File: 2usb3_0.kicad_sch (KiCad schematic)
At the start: 11 parts, among them J5 2xUSB3.0, U3 AP22615AWU

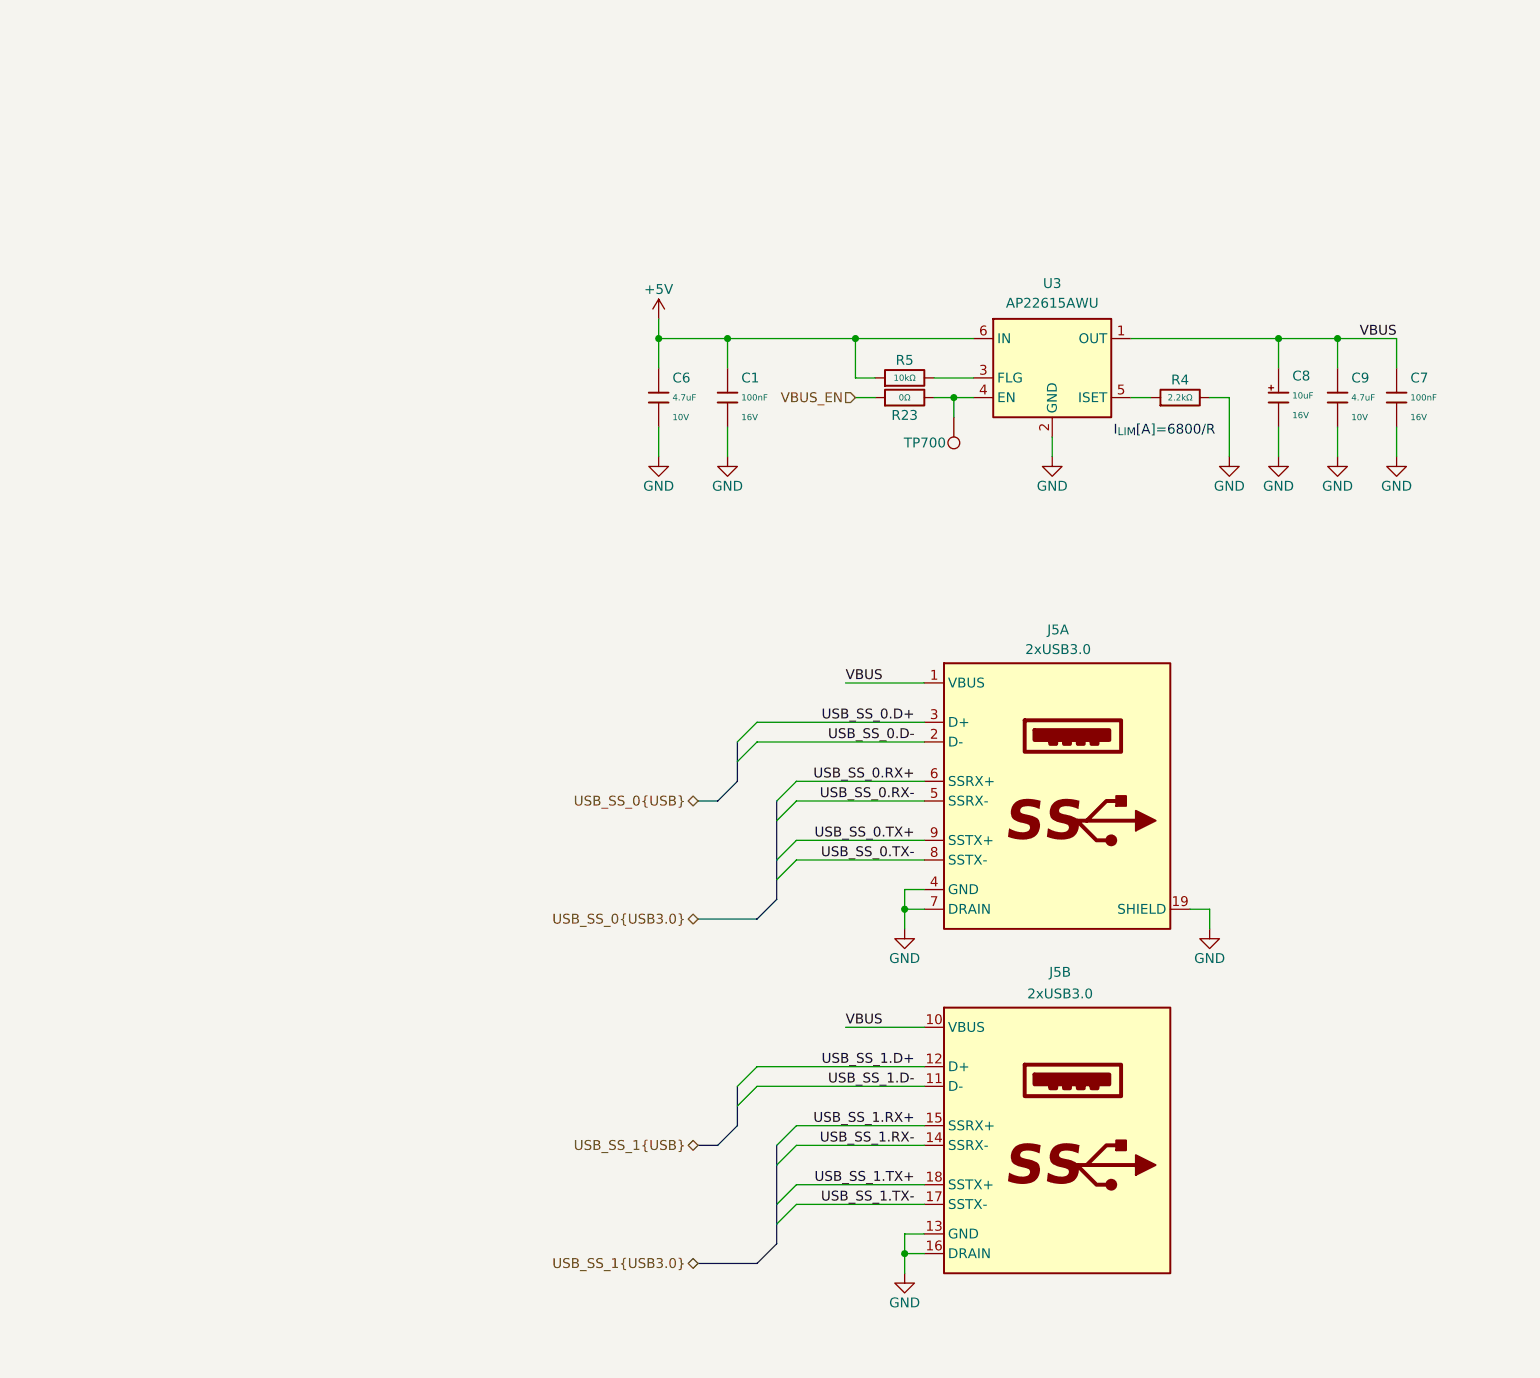
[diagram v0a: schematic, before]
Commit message: [#1] WIP: Change components to ones from the global library, refactor schematic
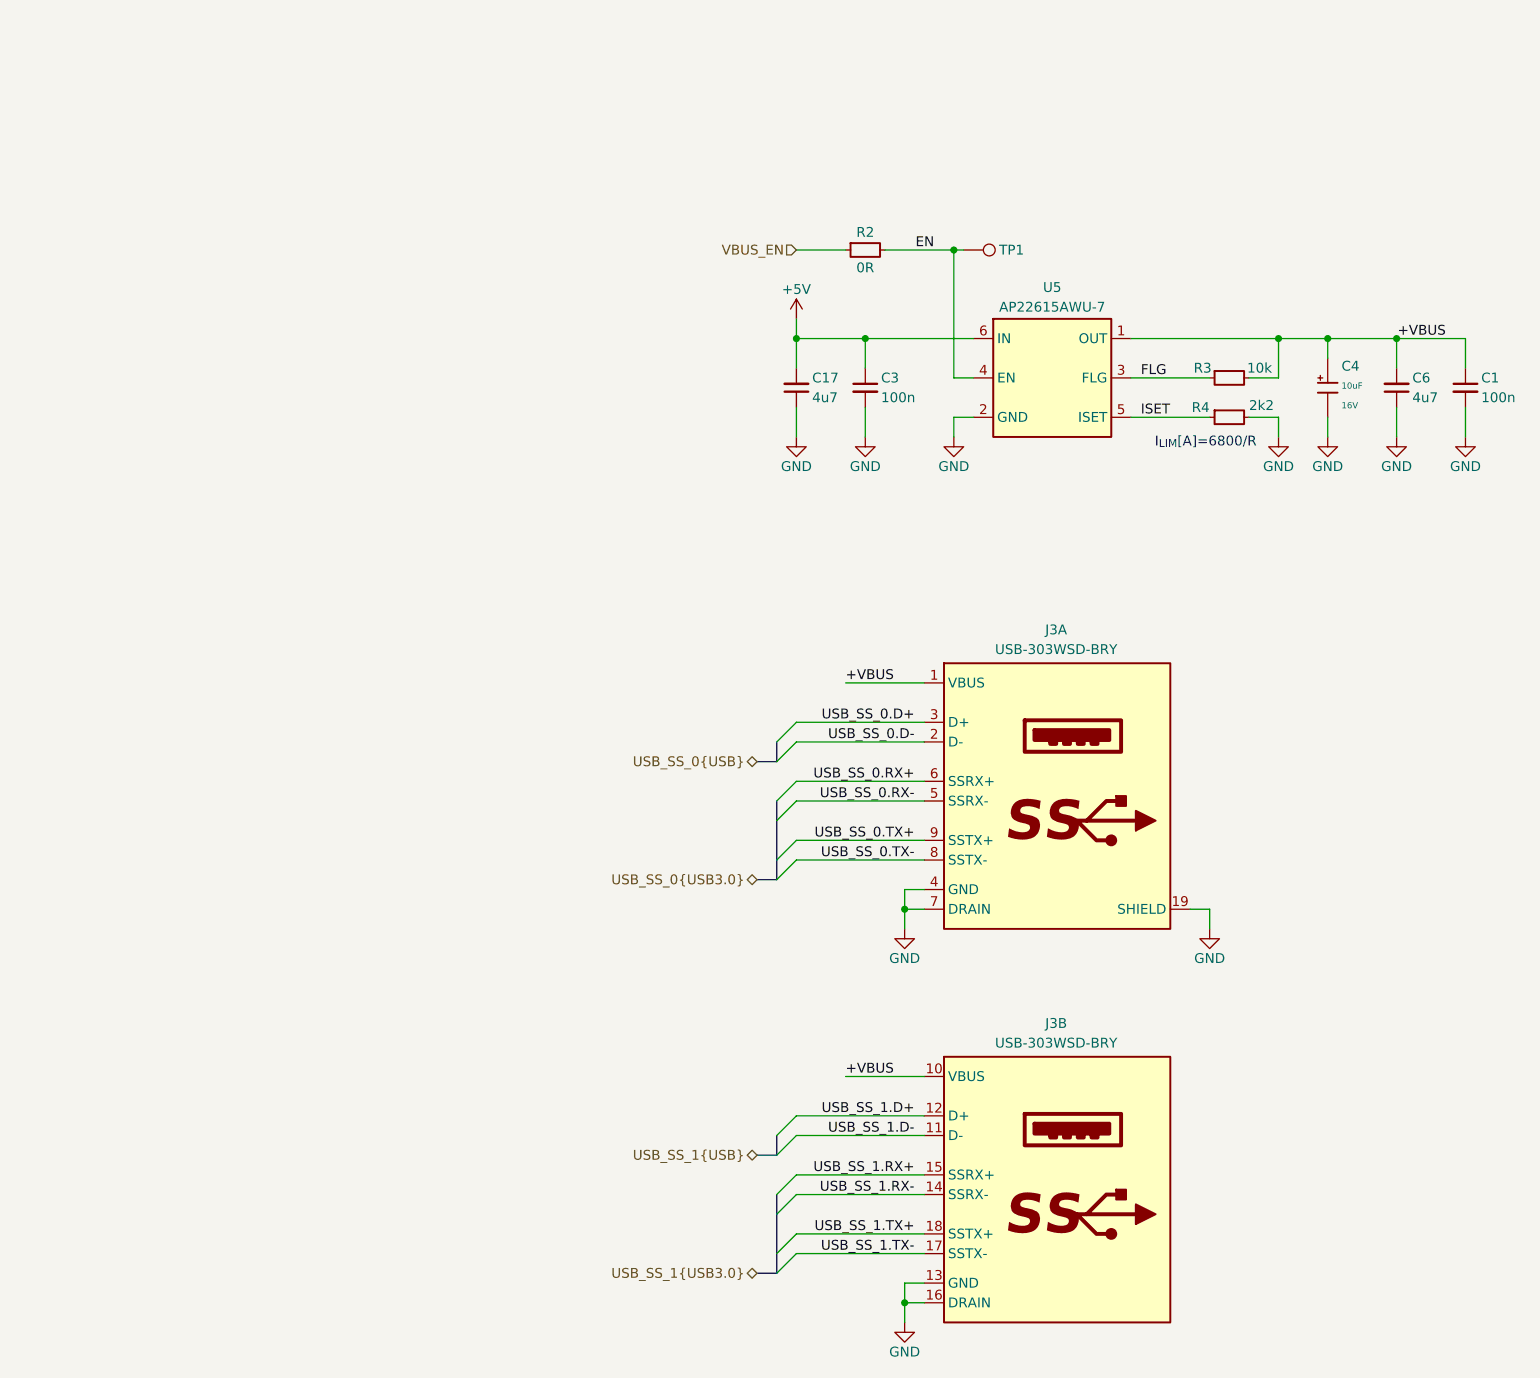
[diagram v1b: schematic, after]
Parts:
- removed C1, C7: 100nF, PCM_JLCPCB:C_0402, symbol PCM_JLCPCB-Capacitors:0402,100nF
- removed C6, C9: 4.7uF, PCM_JLCPCB:C_0402, symbol PCM_JLCPCB-Capacitors:0402,4.7uF
- removed J5: 2xUSB3.0, lib:2xUSB3.0-USB-303WSD-BRY, symbol connectors:2xUSB3.0-USB-303WSD-BRY
- removed R23: 0Ω, PCM_JLCPCB:R_0402, symbol PCM_JLCPCB-Resistors:0402,0Ω
- removed R4: 2.2kΩ, PCM_JLCPCB:R_0402, symbol PCM_JLCPCB-Resistors:0402,2.2kΩ
- removed R5: 10kΩ, PCM_JLCPCB:R_0402, symbol PCM_JLCPCB-Resistors:0402,10kΩ
- removed U3: AP22615AWU, Package_TO_SOT_SMD:SOT-23-6, symbol Regulator_Linear:AP22615AWU
- added C1, C3: C-100n-0402, DW-footprints:C_0402_1005Metric, symbol DW-capacitors:C-100n-0402
- added C17, C6: C-4u7-0402, DW-footprints:C_0402_1005Metric, symbol DW-capacitors:C-4u7-0402
- added J3: USB-A_USB-303WSD-BRY, DW-footprints:USB-A_Receptacle_USB-303WSD-BRY, symbol DW-connectors:USB-A_USB-303WSD-BRY
- added R2: R-0R-0402, DW-footprints:R_0402_1005Metric, symbol DW-resistors:R-0R-0402
- added R3: R-10k-0402, DW-footprints:R_0402_1005Metric, symbol DW-resistors:R-10k-0402
- added R4: R-2k2-0402, DW-footprints:R_0402_1005Metric, symbol DW-resistors:R-2k2-0402
- added U5: AP22615AWU-7, DW-footprints:TSOT-23-6, symbol DW-ICs:AP22615AWU-7
- renumbered C8 to C4, TP700 to TP1
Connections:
- net +5V: now also C17.2, C3.1, U5.6 (IN)
- net GND: now also C1.2, C17.1, C3.2, C6.1, J3.13 (GND), J3.16 (DRAIN), J3.19 (SHIELD), J3.4 (GND), J3.7 (DRAIN), R4.2, U5.2 (GND)
- net USB_SS_0.D+: now also J3.3 (D+)
- net USB_SS_0.D-: now also J3.2 (D-)
- net USB_SS_0.RX+: now also J3.6 (SSRX+)
- net USB_SS_0.RX-: now also J3.5 (SSRX-)
- net USB_SS_0.TX+: now also J3.9 (SSTX+)
- net USB_SS_0.TX-: now also J3.8 (SSTX-)
- net USB_SS_1.D+: now also J3.12 (D+)
- net USB_SS_1.D-: now also J3.11 (D-)
- net USB_SS_1.RX+: now also J3.15 (SSRX+)
- net USB_SS_1.RX-: now also J3.14 (SSRX-)
- net USB_SS_1.TX+: now also J3.18 (SSTX+)
- net USB_SS_1.TX-: now also J3.17 (SSTX-)
- net VBUS_EN: now also R2.1
- net EN: now reaches TP1.1
- net EN: now also R2.2, U5.4 (EN)
- net VBUS renamed +VBUS
- net +VBUS: now also C1.1, C6.2, J3.1 (VBUS), J3.10 (VBUS), R3.2, U5.1 (OUT)
- new net FLG: R3.1, U5.3 (FLG)
- new net ISET: R4.1, U5.5 (ISET)
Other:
- moved on the sheet: C4, TP1

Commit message: [#1] Re-annotate schematic
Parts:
- removed TP1: TestPoint, TestPoint:TestPoint_Pad_D1.0mm, symbol Connector:TestPoint
- added TP7: TP_SMD_0.75mm, DW-footprints:TP_SMD_0.75mm, symbol DW-test-points:TP_SMD_0.75mm
- renumbered C1 to C4, C4 to C5, C17 to C6, C6 to C7, J3 to J7, R2 to R10, R3 to R11, R4 to R12, U5 to U1
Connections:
- net EN: now also TP7.1
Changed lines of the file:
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@@
 		(on_board yes)
 		(dnp no)
-		(property "Reference" "#PWR24"
+		(property "Reference" "#PWR034"
 			(at 199.39 90.17 0)
 			(effects
@@
 			(project "cm5-module"
 				(path "/090a8e41-87a8-4fb1-998b-60a2c0dc4cee/658b004a-eb7c-4ad1-a8df-d1cd97b62092"
-					(reference "#PWR24")
+					(reference "#PWR034")
 					(unit 1)
 				)
@@
 		(on_board yes)
 		(dnp no)
-		(property "Reference" "R2"
+		(property "Reference" "R10"
 			(at 199.39 57.404 0)
 			(effects
@@
 			(project ""
 				(path "/090a8e41-87a8-4fb1-998b-60a2c0dc4cee/658b004a-eb7c-4ad1-a8df-d1cd97b62092"
-					(reference "R2")
+					(reference "R10")
 					(unit 1)
 				)
@@
 		(on_board yes)
 		(dnp no)
-		(property "Reference" "#PWR25"
+		(property "Reference" "#PWR035"
 			(at 210.82 90.17 0)
 			(effects
@@
 			(project "cm5-module"
 				(path "/090a8e41-87a8-4fb1-998b-60a2c0dc4cee/658b004a-eb7c-4ad1-a8df-d1cd97b62092"
-					(reference "#PWR25")
+					(reference "#PWR035")
 					(unit 1)
 				)
@@
 		(on_board yes)
 		(dnp no)
-		(property "Reference" "R3"
+		(property "Reference" "R11"
 			(at 244.094 74.93 0)
 			(effects
@@
 			(project ""
 				(path "/090a8e41-87a8-4fb1-998b-60a2c0dc4cee/658b004a-eb7c-4ad1-a8df-d1cd97b62092"
-					(reference "R3")
+					(reference "R11")
 					(unit 1)
 				)
@@
 		(on_board yes)
 		(dnp no)
-		(property "Reference" "#PWR27"
+		(property "Reference" "#PWR037"
 			(at 259.08 90.17 0)
 			(effects
@@
 			(project "cm5-module"
 				(path "/090a8e41-87a8-4fb1-998b-60a2c0dc4cee/658b004a-eb7c-4ad1-a8df-d1cd97b62092"
-					(reference "#PWR27")
+					(reference "#PWR037")
 					(unit 1)
 				)
@@
 		(on_board yes)
 		(dnp no)
-		(property "Reference" "#PWR32"
+		(property "Reference" "#PWR042"
 			(at 204.47 204.47 0)
 			(effects
@@
 			(project "cm5-module"
 				(path "/090a8e41-87a8-4fb1-998b-60a2c0dc4cee/658b004a-eb7c-4ad1-a8df-d1cd97b62092"
-					(reference "#PWR32")
+					(reference "#PWR042")
 					(unit 1)
 				)
@@
 		(on_board yes)
 		(dnp no)
-		(property "Reference" "U5"
+		(property "Reference" "U1"
 			(at 223.52 64.516 0)
 			(effects
@@
 			(project ""
 				(path "/090a8e41-87a8-4fb1-998b-60a2c0dc4cee/658b004a-eb7c-4ad1-a8df-d1cd97b62092"
-					(reference "U5")
+					(reference "U1")
 					(unit 1)
 				)
@@
 		(on_board yes)
 		(dnp no)
-		(property "Reference" "R4"
+		(property "Reference" "R12"
 			(at 243.84 80.01 0)
 			(effects
@@
 			(project ""
 				(path "/090a8e41-87a8-4fb1-998b-60a2c0dc4cee/658b004a-eb7c-4ad1-a8df-d1cd97b62092"
-					(reference "R4")
+					(reference "R12")
 					(unit 1)
 				)
@@
 		(on_board yes)
 		(dnp no)
-		(property "Reference" "#PWR014"
+		(property "Reference" "#PWR032"
 			(at 190.5 72.39 0)
 			(effects
@@
 			(project ""
 				(path "/090a8e41-87a8-4fb1-998b-60a2c0dc4cee/658b004a-eb7c-4ad1-a8df-d1cd97b62092"
-					(reference "#PWR014")
+					(reference "#PWR032")
 					(unit 1)
 				)
@@
 		(on_board yes)
 		(dnp no)
-		(property "Reference" "C4"
+		(property "Reference" "C5"
 			(at 260.858 74.6759 0)
 			(effects
@@
 			(project ""
 				(path "/090a8e41-87a8-4fb1-998b-60a2c0dc4cee/658b004a-eb7c-4ad1-a8df-d1cd97b62092"
-					(reference "C4")
+					(reference "C5")
 					(unit 1)
 				)
@@
 		(on_board yes)
 		(dnp no)
-		(property "Reference" "#PWR31"
+		(property "Reference" "#PWR041"
 			(at 243.84 153.67 0)
 			(effects
@@
 			(project "cm5-module"
 				(path "/090a8e41-87a8-4fb1-998b-60a2c0dc4cee/658b004a-eb7c-4ad1-a8df-d1cd97b62092"
-					(reference "#PWR31")
+					(reference "#PWR041")
 					(unit 1)
 				)
@@
 		(on_board yes)
 		(dnp no)
-		(property "Reference" "#PWR26"
+		(property "Reference" "#PWR036"
 			(at 252.73 90.17 0)
 			(effects
@@
 			(project "cm5-module"
 				(path "/090a8e41-87a8-4fb1-998b-60a2c0dc4cee/658b004a-eb7c-4ad1-a8df-d1cd97b62092"
-					(reference "#PWR26")
+					(reference "#PWR036")
 					(unit 1)
 				)
@@
 		(on_board yes)
 		(dnp no)
-		(property "Reference" "C17"
+		(property "Reference" "C6"
 			(at 192.532 76.2 90)
 			(effects
@@
 			(project "cm5-module"
 				(path "/090a8e41-87a8-4fb1-998b-60a2c0dc4cee/658b004a-eb7c-4ad1-a8df-d1cd97b62092"
-					(reference "C17")
+					(reference "C6")
 					(unit 1)
 				)
@@
 		(on_board yes)
 		(dnp no)
-		(property "Reference" "C6"
+		(property "Reference" "C7"
 			(at 270.002 76.2 90)
 			(effects
@@
 			(project ""
 				(path "/090a8e41-87a8-4fb1-998b-60a2c0dc4cee/658b004a-eb7c-4ad1-a8df-d1cd97b62092"
-					(reference "C6")
+					(reference "C7")
 					(unit 1)
 				)
@@
 		(on_board yes)
 		(dnp no)
-		(property "Reference" "J3"
+		(property "Reference" "J7"
 			(at 224.028 159.512 0)
 			(effects
@@
 			(project ""
 				(path "/090a8e41-87a8-4fb1-998b-60a2c0dc4cee/658b004a-eb7c-4ad1-a8df-d1cd97b62092"
-					(reference "J3")
+					(reference "J7")
 					(unit 2)
 				)
@@
 	)
 	(symbol
-		(lib_id "Connector:TestPoint")
-		(at 212.09 59.69 270)
+		(lib_id "DW-test-points:TP_SMD_0.75mm")
+		(at 212.09 59.69 0)
 		(unit 1)
 		(exclude_from_sim no)
-		(in_bom yes)
+		(in_bom no)
 		(on_board yes)
 		(dnp no)
-		(property "Reference" "TP1"
-			(at 216.662 59.69 90)
-			(effects
-				(font
-					(size 1.27 1.27)
+		(property "Reference" "TP7"
+			(at 214.884 59.69 0)
+			(effects
+				(font
+					(size 1.27 1.27)
+					(thickness 0.15)
 				)
 				(justify left)
 			)
 		)
-		(property "Value" "TestPoint"
-			(at 217.17 60.9599 90)
-			(effects
-				(font
-					(size 1.27 1.27)
-				)
-				(justify left)
-				(hide yes)
-			)
-		)
-		(property "Footprint" "TestPoint:TestPoint_Pad_D1.0mm"
-			(at 212.09 64.77 0)
-			(effects
-				(font
-					(size 1.27 1.27)
-				)
-				(hide yes)
-			)
-		)
-		(property "Datasheet" "~"
-			(at 212.09 64.77 0)
-			(effects
-				(font
-					(size 1.27 1.27)
-				)
-				(hide yes)
-			)
-		)
-		(property "Description" "test point"
-			(at 212.09 59.69 0)
-			(effects
-				(font
-					(size 1.27 1.27)
-				)
+		(property "Value" "TP_SMD_0.75mm"
+			(at 215.9 62.23 0)
+			(effects
+				(font
+					(size 1.27 1.27)
+					(thickness 0.15)
+				)
+				(justify left bottom)
+				(hide yes)
+			)
+		)
+		(property "Footprint" "DW-footprints:TP_SMD_0.75mm"
+			(at 215.9 64.77 0)
+			(effects
+				(font
+					(size 1.27 1.27)
+					(thickness 0.15)
+				)
+				(justify left bottom)
+				(hide yes)
+			)
+		)
+		(property "Datasheet" ""
+			(at 215.9 67.31 0)
+			(effects
+				(font
+					(size 1.27 1.27)
+					(thickness 0.15)
+				)
+				(justify left bottom)
+				(hide yes)
+			)
+		)
+		(property "Description" "Test point, SMD, round, 0.75mm diameter"
+			(at 215.9 69.85 0)
+			(effects
+				(font
+					(size 1.27 1.27)
+					(thickness 0.15)
+				)
+				(justify left bottom)
 				(hide yes)
 			)
@@
 			(project "cm5-module"
 				(path "/090a8e41-87a8-4fb1-998b-60a2c0dc4cee/658b004a-eb7c-4ad1-a8df-d1cd97b62092"
-					(reference "TP1")
+					(reference "TP7")
 					(unit 1)
 				)
@@
 		(on_board yes)
 		(dnp no)
-		(property "Reference" "#PWR30"
+		(property "Reference" "#PWR040"
 			(at 204.47 153.67 0)
 			(effects
@@
 			(project "cm5-module"
 				(path "/090a8e41-87a8-4fb1-998b-60a2c0dc4cee/658b004a-eb7c-4ad1-a8df-d1cd97b62092"
-					(reference "#PWR30")
+					(reference "#PWR040")
 					(unit 1)
 				)
@@
 		(on_board yes)
 		(dnp no)
-		(property "Reference" "#PWR29"
+		(property "Reference" "#PWR039"
 			(at 276.86 90.17 0)
 			(effects
@@
 			(project "cm5-module"
 				(path "/090a8e41-87a8-4fb1-998b-60a2c0dc4cee/658b004a-eb7c-4ad1-a8df-d1cd97b62092"
-					(reference "#PWR29")
+					(reference "#PWR039")
 					(unit 1)
 				)
@@
 		(on_board yes)
 		(dnp no)
-		(property "Reference" "C1"
+		(property "Reference" "C4"
 			(at 278.892 76.2 90)
 			(effects
@@
 			(project ""
 				(path "/090a8e41-87a8-4fb1-998b-60a2c0dc4cee/658b004a-eb7c-4ad1-a8df-d1cd97b62092"
-					(reference "C1")
+					(reference "C4")
 					(unit 1)
 				)
@@
 		(on_board yes)
 		(dnp no)
-		(property "Reference" "#PWR23"
+		(property "Reference" "#PWR033"
 			(at 190.5 90.17 0)
 			(effects
@@
 			(project "cm5-module"
 				(path "/090a8e41-87a8-4fb1-998b-60a2c0dc4cee/658b004a-eb7c-4ad1-a8df-d1cd97b62092"
-					(reference "#PWR23")
+					(reference "#PWR033")
 					(unit 1)
 				)
@@
 		(on_board yes)
 		(dnp no)
-		(property "Reference" "#PWR28"
+		(property "Reference" "#PWR038"
 			(at 267.97 90.17 0)
 			(effects
@@
 			(project "cm5-module"
 				(path "/090a8e41-87a8-4fb1-998b-60a2c0dc4cee/658b004a-eb7c-4ad1-a8df-d1cd97b62092"
-					(reference "#PWR28")
+					(reference "#PWR038")
 					(unit 1)
 				)
@@
 		(on_board yes)
 		(dnp no)
-		(property "Reference" "J3"
+		(property "Reference" "J7"
 			(at 224.028 108.712 0)
 			(effects
@@
 			(project ""
 				(path "/090a8e41-87a8-4fb1-998b-60a2c0dc4cee/658b004a-eb7c-4ad1-a8df-d1cd97b62092"
-					(reference "J3")
+					(reference "J7")
 					(unit 1)
 				)
